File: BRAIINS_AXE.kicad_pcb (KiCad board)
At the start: 6 copper layers, 105.5 x 181.1 mm, 273 parts, among them J1 RJ45_Hanrun_HR911105A_Horizon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, J10 Connector 02x01, J2 Conn_01x06, J9 Conn_01x10, M1 Fan_4pin, M2 Fan_4pin, U10 BM1370_mode1, U11 BM1370_mode1, U12 W5500, U16 CSD95472Q5MC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

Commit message: rp2350 module in place
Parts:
- added A1: RaspberryPi_Pico, Module:RaspberryPi_Pico_Common_Unspecified, F.Cu at (115.9, 64.1)
- moved U30 144.1 mm to (242.2, 104.0)
- moved D3 67.1 mm to (182.3, 91.0)
- moved C137 56.0 mm to (201.4, 65.0)
- moved C138 56.0 mm to (201.4, 67.5)
- moved C139 56.0 mm to (201.4, 70.0)
- moved C140 56.0 mm to (201.4, 72.6)
- moved C141 56.0 mm to (201.4, 75.1)
- moved C142 56.0 mm to (201.4, 77.6)
- moved R41 56.0 mm to (201.4, 80.1)
- moved R42 56.0 mm to (201.4, 82.6)
- moved R45 56.0 mm to (201.4, 85.1)
- moved X1 56.0 mm to (214.1, 80.8)
- moved C128 56.0 mm to (197.4, 65.0)
- moved C129 56.0 mm to (197.4, 67.5)
- moved C130 56.0 mm to (197.4, 70.0)
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
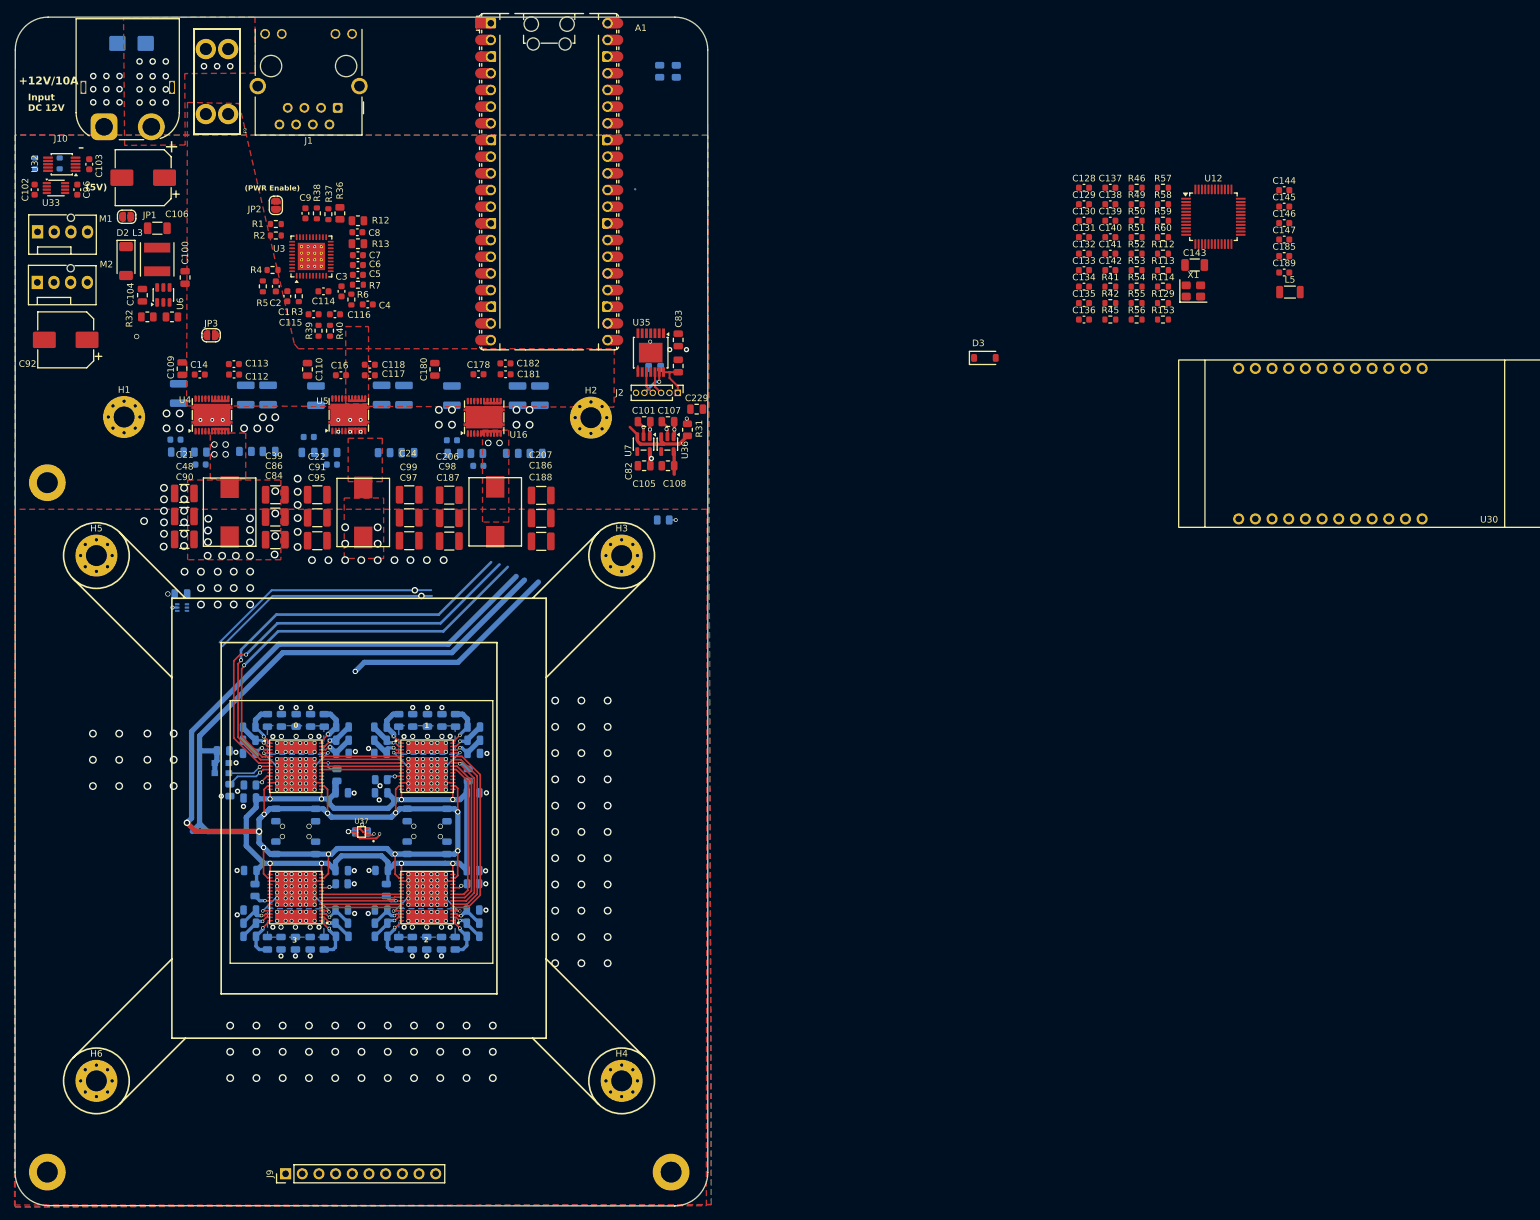
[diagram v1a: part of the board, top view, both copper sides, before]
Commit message: placing W5500
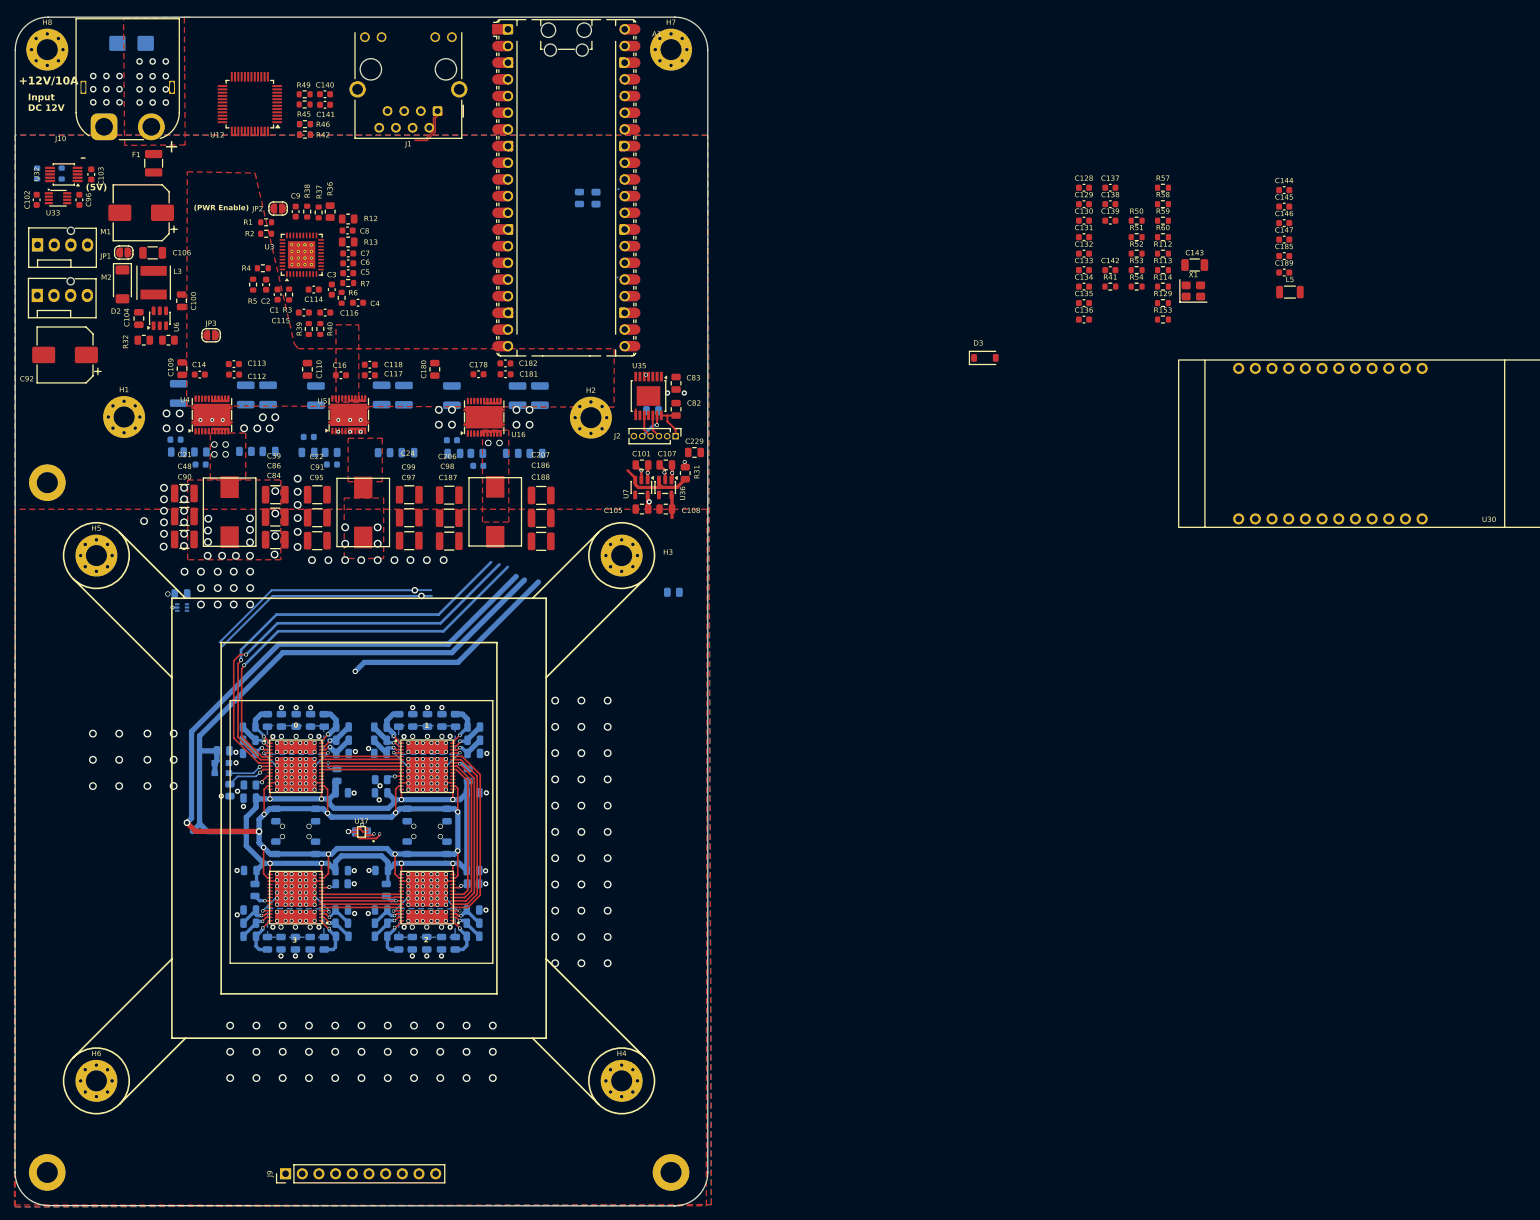
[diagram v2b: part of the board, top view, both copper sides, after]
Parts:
- removed F9: XFCN XF-508P-B, Nerd8:XFCN XF-508P-B
- added F1: Bourns SF-1206HHA1500R-2, Fuse:Fuse_1210_3225Metric, F.Cu at (55.7, 61.3)
- added H7: MountingHole, MountingHole:MountingHole_3.2mm_M3_Pad_Via, F.Cu at (134.5, 44.0)
- added H8: MountingHole, MountingHole:MountingHole_3.2mm_M3_Pad_Via, F.Cu at (39.5, 44.0)
- R55, R56: moved to B.Cu
- moved U12 147.7 mm to (70.3, 52.3), turned to 180 degrees
- moved R56 129.8 mm to (78.8, 57.0), turned to 180 degrees
- moved R55 129.6 mm to (78.8, 55.4), turned to 180 degrees
- moved R49 127.8 mm to (78.7, 50.8)
- moved R46 127.0 mm to (78.8, 55.4)
- moved R45 127.0 mm to (78.7, 52.4)
- moved R42 125.3 mm to (78.8, 57.0)
- moved C141 121.7 mm to (81.8, 52.4)
- moved C140 121.6 mm to (81.8, 50.8)
- moved R44 22.9 mm to (123.1, 66.6)
- moved R43 22.9 mm to (120.5, 66.6)
- moved J1 15.2 mm to (98.9, 53.4)
- moved R29 11.1 mm to (134.8, 126.7)
- moved C83 6.61 mm to (135.3, 94.8)
- moved J2 6.61 mm to (135.2, 102.9)
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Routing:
- net /controller/ETH_TX_P: track 0.00 -> 7.15 mm
- net /controller/ETH_TX_N: track 0.00 -> 7.03 mm
- net VDD: track 1.00 -> 0.00 mm, vias 148 -> 147
- net Net-(D1-A1): vias 15 -> 12
- net +12V: vias 1 -> 0

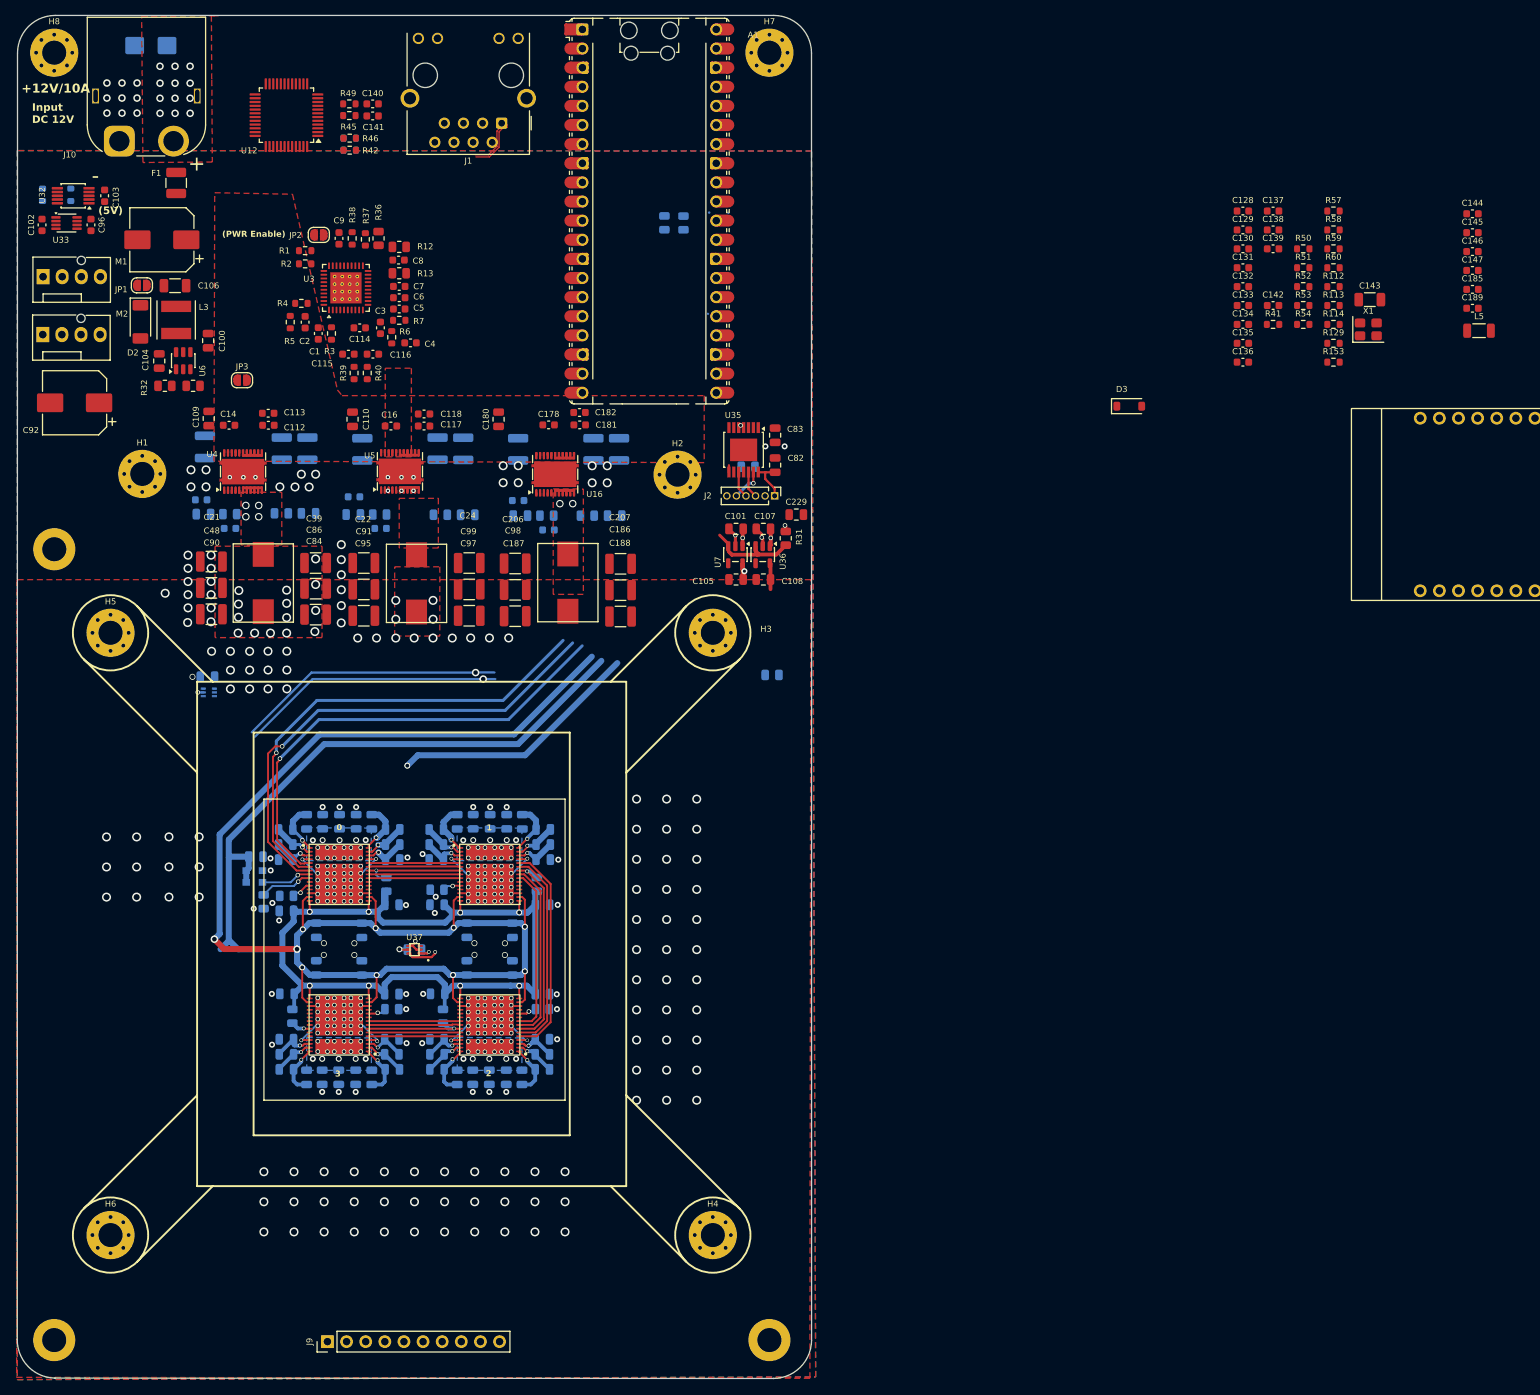
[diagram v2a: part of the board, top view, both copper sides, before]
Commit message: w5500 placed
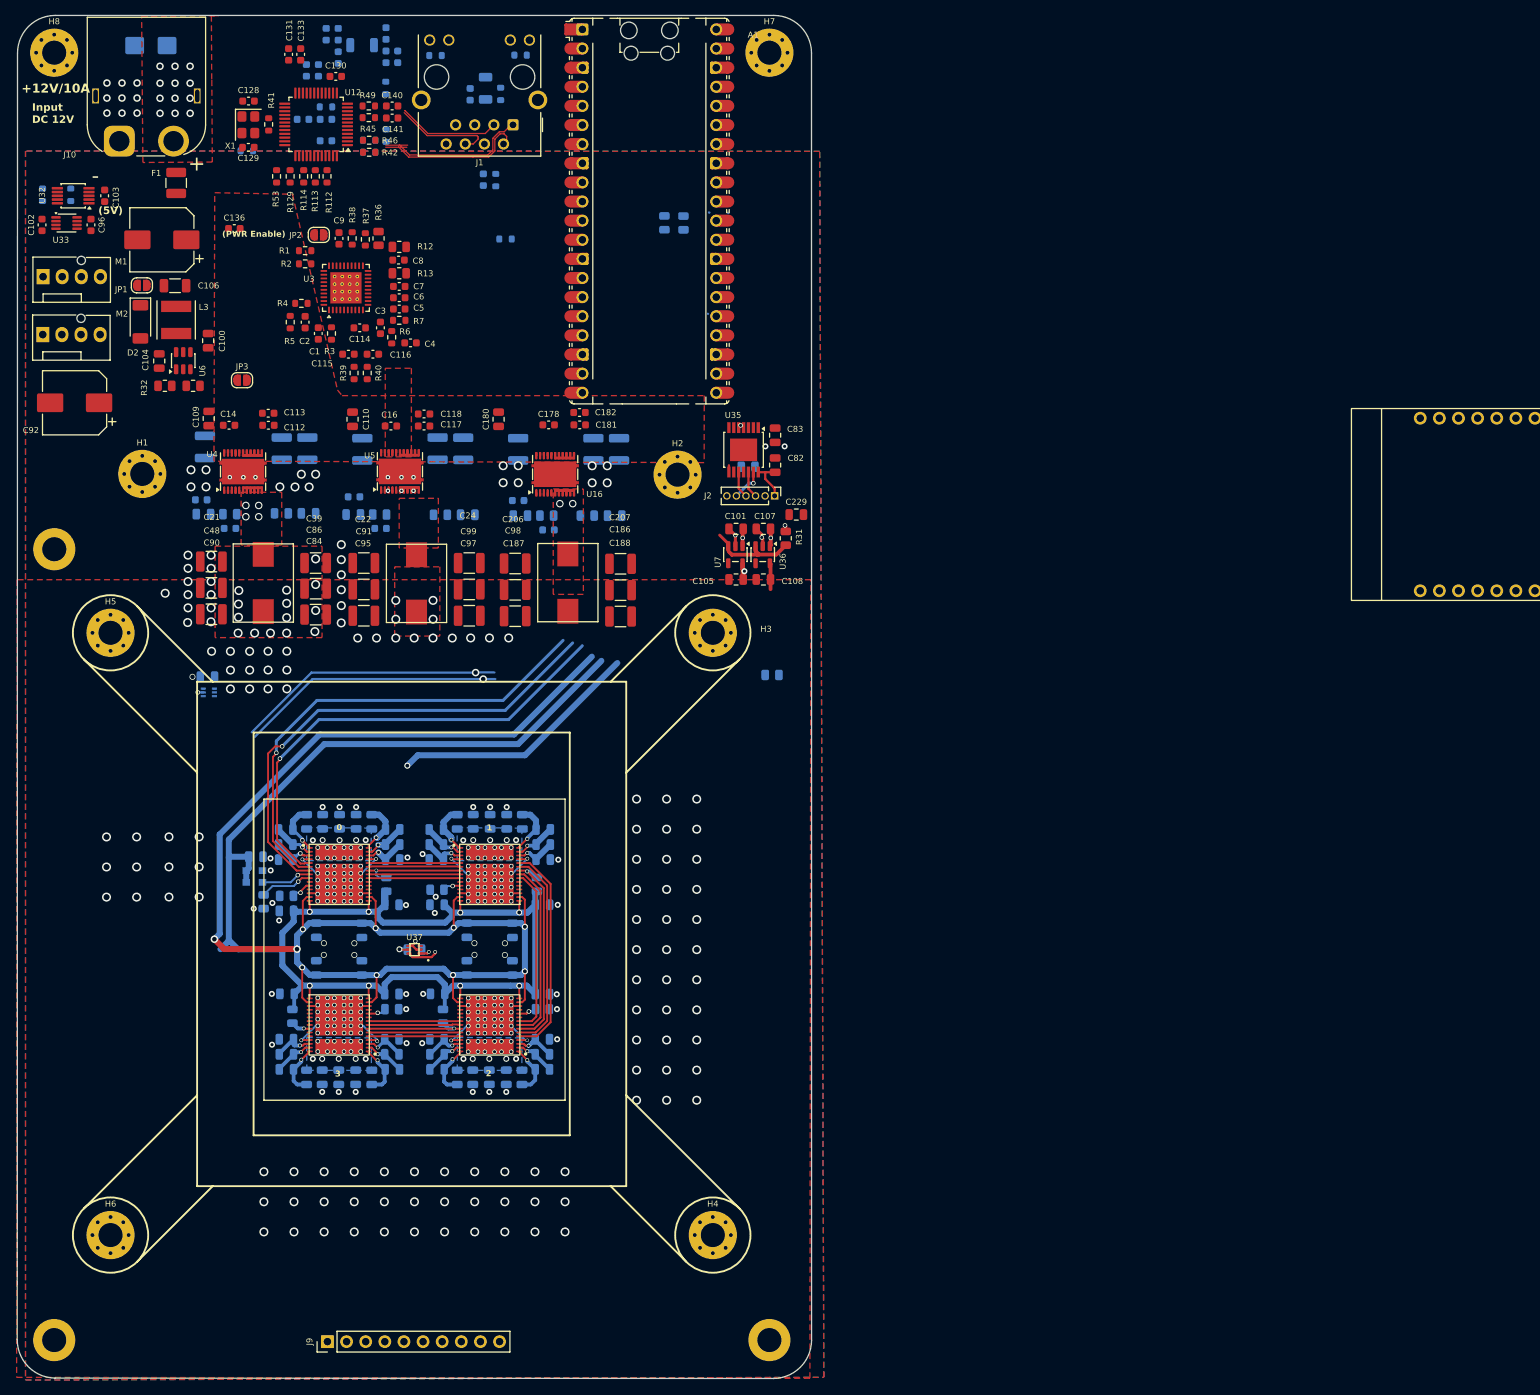
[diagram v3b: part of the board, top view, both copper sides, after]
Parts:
- removed D3: 1N5819, Diode_SMD:D_SOD-123
- C132, C134, C135, C137, C138, C139, C142, C144, C145, C146, C147, C185, C189, L5, R153, R50, R51, R52, R54, R57, R58, R59, R60: moved to B.Cu
- C143: value 1n -> 1nF/2kV; moved to B.Cu
- moved C146 155.0 mm to (75.6, 41.5), turned to 90 degrees
- moved C189 154.3 mm to (77.2, 44.6), turned to -90 degrees
- moved C147 153.9 mm to (77.2, 41.5), turned to 90 degrees
- moved L5 153.1 mm to (80.4, 43.0), turned to 180 degrees
- moved X1 151.2 mm to (65.3, 53.6), turned to -90 degrees
- moved C185 147.6 mm to (83.6, 44.5), turned to -90 degrees
- moved C144 146.3 mm to (83.6, 41.5), turned to 90 degrees
- moved C145 144.7 mm to (85.1, 44.5), turned to -90 degrees
- moved R52 141.5 mm to (65.1, 57.0), turned to 180 degrees
- moved R129 140.3 mm to (70.8, 60.4), turned to -90 degrees
- moved R114 138.2 mm to (72.6, 60.4), turned to -90 degrees
- moved R53 137.4 mm to (69.0, 60.4), turned to -90 degrees
- moved R113 136.3 mm to (74.2, 60.4), turned to -90 degrees
- moved R41 136.0 mm to (68.0, 53.5), turned to -90 degrees
- moved C136 135.1 mm to (63.4, 67.4)
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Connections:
- C143 pad 2: unconnected-(C143-Pad2) -> FGND
- U30 pad 12: Net-(D3-K) -> unconnected-(U30-5V-Pad12)
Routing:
- net /controller/ETH_TX_N: track 7.03 -> 21.2 mm
- net /controller/ETH_TX_P: track 7.15 -> 21.1 mm
- net /controller/ETH_RX_P: track 0.00 -> 13.6 mm
- net /controller/ETH_RX_N: track 0.00 -> 13.4 mm
